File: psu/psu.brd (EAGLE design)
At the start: 31 x 67 mm, 8 parts

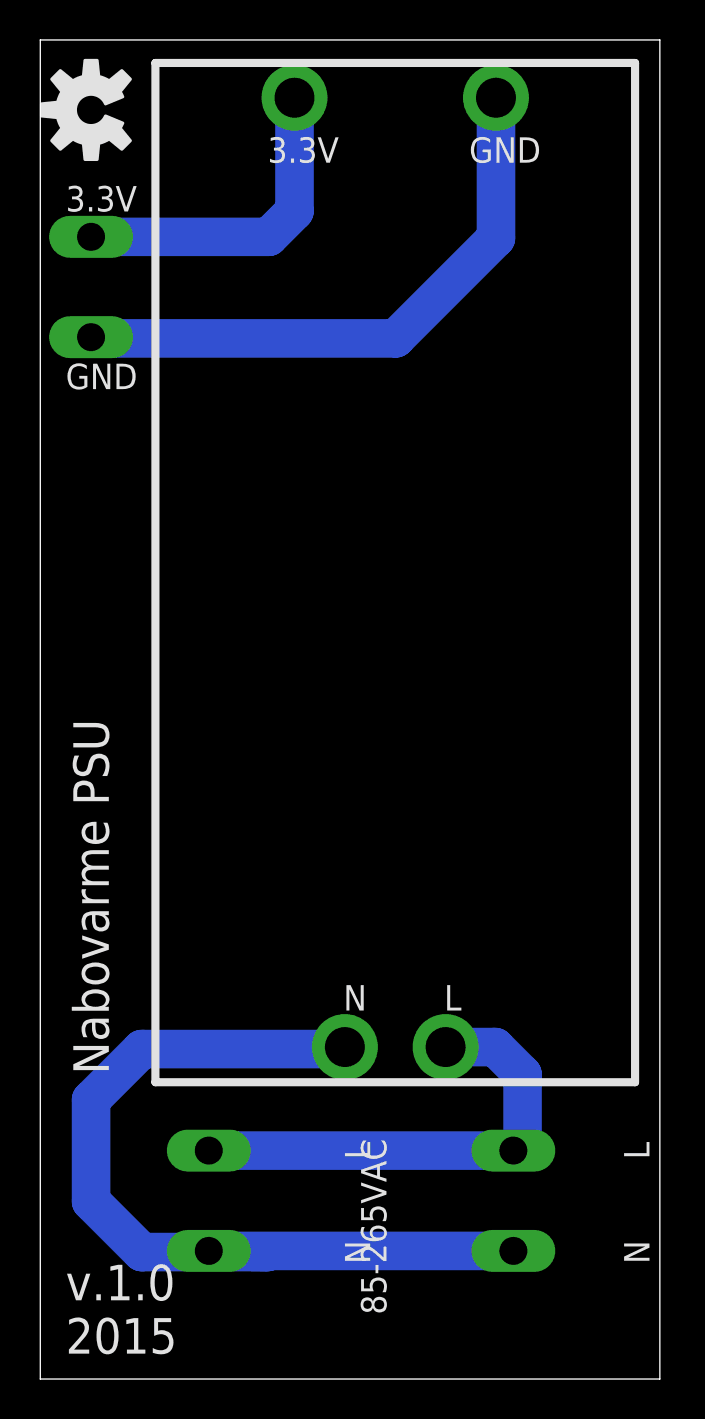
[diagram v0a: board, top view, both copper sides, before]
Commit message: psu pcb: v1.1
better placement of holes for psu module
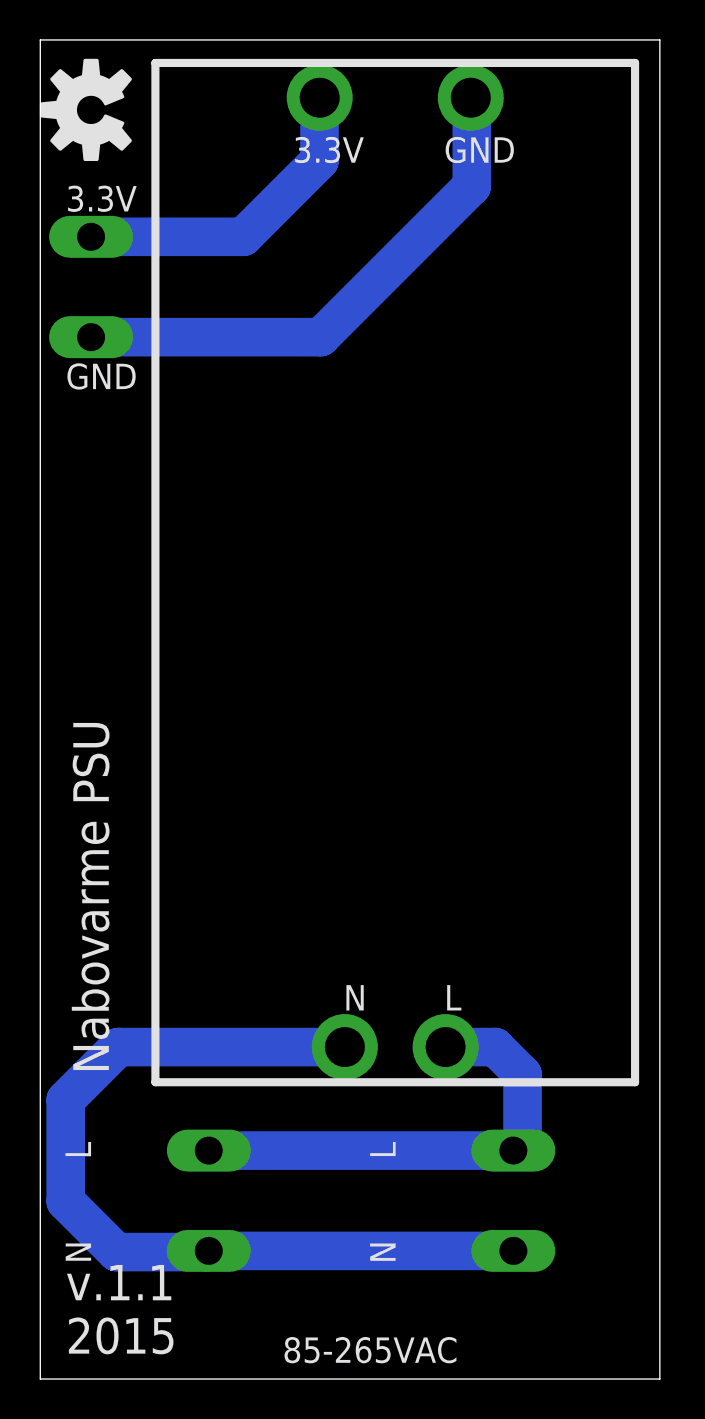
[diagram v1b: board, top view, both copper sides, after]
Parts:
- moved GND 1.26 mm to (21.5, 64.1)
- moved 3.3V 1.26 mm to (14.0, 64.1)
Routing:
- net N$2: track 46.9 -> 43.6 mm
- net N$4: track 29.4 -> 26.6 mm
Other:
- board text added: "v.1.1 2015"
- board text removed: "v.1.0 2015"
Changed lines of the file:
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@@
 <text x="1.27" y="58.42" size="1.27" layer="25">3.3V</text>
 <text x="1.27" y="50.8" size="1.27" layer="25" align="top-left">GND</text>
-<text x="1.27" y="1.27" size="1.778" layer="25">v.1.0
+<text x="1.27" y="1.27" size="1.778" layer="25">v.1.1
 2015</text>
-<text x="16.51" y="11.43" size="1.27" layer="25" rot="R270" align="top-center">L</text>
-<text x="16.51" y="6.35" size="1.27" layer="25" rot="R270" align="top-center">N</text>
-<text x="29.21" y="6.35" size="1.27" layer="25" rot="R90" align="top-center">N</text>
-<text x="29.21" y="11.43" size="1.27" layer="25" rot="R90" align="top-center">L</text>
+<text x="2.54" y="11.43" size="1.27" layer="25" rot="R270" align="top-center">L</text>
+<text x="2.54" y="6.35" size="1.27" layer="25" rot="R270" align="top-center">N</text>
+<text x="16.51" y="6.35" size="1.27" layer="25" rot="R90" align="top-center">N</text>
+<text x="16.51" y="11.43" size="1.27" layer="25" rot="R90" align="top-center">L</text>
 </plain>
 <attributes>
@@
 <attribute name="NAME" x="20.2038" y="18.4388" size="1.27" layer="25"/>
 </element>
-<element name="3.3V" library="SparkFun (old)" package="1X01_2MM" value="M01PTH_2MM" x="12.72" y="64.11" smashed="yes">
-<attribute name="NAME" x="11.3738" y="60.8588" size="1.27" layer="25"/>
-</element>
-<element name="GND" library="SparkFun (old)" package="1X01_2MM" value="M01PTH_2MM" x="22.8" y="64.11" smashed="yes">
-<attribute name="NAME" x="21.4538" y="60.8588" size="1.27" layer="25"/>
+<element name="3.3V" library="SparkFun (old)" package="1X01_2MM" value="M01PTH_2MM" x="13.98" y="64.11" smashed="yes">
+<attribute name="NAME" x="12.6338" y="60.8588" size="1.27" layer="25"/>
+</element>
+<element name="GND" library="SparkFun (old)" package="1X01_2MM" value="M01PTH_2MM" x="21.54" y="64.11" smashed="yes">
+<attribute name="NAME" x="20.1938" y="60.8588" size="1.27" layer="25"/>
 </element>
 <element name="85-265VAC" library="SparkFun (old)" package="1X02_LONGPADS" value="" x="23.67" y="11.43" smashed="yes" rot="R270">
-<attribute name="NAME" x="16.05" y="7.62" size="1.27" layer="25" rot="R270" align="bottom-center"/>
+<attribute name="NAME" x="16.51" y="0.81" size="1.27" layer="25" align="bottom-center"/>
 </element>
 <element name="JP2" library="SparkFun (old)" package="1X02_LONGPADS" value="" x="2.54" y="57.15" smashed="yes" rot="R270"/>
@@
 <contactref element="N" pad="1"/>
 <contactref element="85-265VAC1" pad="2"/>
-<wire x1="5.08" y1="6.35" x2="11.37" y2="6.35" width="1.9304" layer="16"/>
-<wire x1="11.37" y1="6.35" x2="8.43" y2="6.41" width="1.9304" layer="16"/>
-<wire x1="8.43" y1="6.41" x2="23.67" y2="6.41" width="1.9304" layer="16"/>
-<wire x1="5.08" y1="6.35" x2="2.54" y2="8.89" width="1.9304" layer="16"/>
-<wire x1="2.54" y1="8.89" x2="2.54" y2="13.97" width="1.9304" layer="16"/>
-<wire x1="2.54" y1="13.97" x2="5.08" y2="16.51" width="1.9304" layer="16"/>
-<wire x1="5.08" y1="16.51" x2="15.14" y2="16.51" width="1.9304" layer="16"/>
-<wire x1="15.14" y1="16.51" x2="15.24" y2="16.61" width="1.9304" layer="16"/>
+<wire x1="15.24" y1="16.61" x2="3.91" y2="16.61" width="1.9304" layer="16"/>
+<wire x1="3.91" y1="16.61" x2="1.27" y2="13.97" width="1.9304" layer="16"/>
+<wire x1="1.27" y1="13.97" x2="1.27" y2="8.89" width="1.9304" layer="16"/>
+<wire x1="1.27" y1="8.89" x2="3.81" y2="6.35" width="1.9304" layer="16"/>
+<wire x1="3.81" y1="6.35" x2="8.37" y2="6.35" width="1.9304" layer="16"/>
+<wire x1="8.37" y1="6.35" x2="8.43" y2="6.41" width="1.9304" layer="16"/>
+<wire x1="23.67" y1="6.41" x2="8.43" y2="6.41" width="1.9304" layer="16"/>
 </signal>
 <signal name="N$3">
 <contactref element="JP2" pad="1"/>
 <contactref element="3.3V" pad="1"/>
-<wire x1="12.72" y1="64.11" x2="12.72" y2="58.44" width="1.9304" layer="16"/>
-<wire x1="12.72" y1="58.44" x2="11.43" y2="57.15" width="1.9304" layer="16"/>
-<wire x1="11.43" y1="57.15" x2="2.54" y2="57.15" width="1.9304" layer="16"/>
+<wire x1="2.54" y1="57.15" x2="10.16" y2="57.15" width="1.9304" layer="16"/>
+<wire x1="10.16" y1="57.15" x2="13.97" y2="60.96" width="1.9304" layer="16"/>
+<wire x1="13.97" y1="60.96" x2="13.97" y2="64.1" width="1.9304" layer="16"/>
+<wire x1="13.97" y1="64.1" x2="13.98" y2="64.11" width="1.9304" layer="16"/>
 </signal>
 <signal name="N$4">
 <contactref element="JP2" pad="2"/>
 <contactref element="GND" pad="1"/>
-<wire x1="22.8" y1="64.11" x2="22.8" y2="57.09" width="1.9304" layer="16"/>
-<wire x1="22.8" y1="57.09" x2="17.78" y2="52.07" width="1.9304" layer="16"/>
-<wire x1="17.78" y1="52.07" x2="2.6" y2="52.07" width="1.9304" layer="16"/>
-<wire x1="2.6" y1="52.07" x2="2.54" y2="52.13" width="1.9304" layer="16"/>
+<wire x1="2.54" y1="52.13" x2="14.03" y2="52.13" width="1.9304" layer="16"/>
+<wire x1="14.03" y1="52.13" x2="21.59" y2="59.69" width="1.9304" layer="16"/>
+<wire x1="21.59" y1="59.69" x2="21.59" y2="64.06" width="1.9304" layer="16"/>
+<wire x1="21.59" y1="64.06" x2="21.54" y2="64.11" width="1.9304" layer="16"/>
 </signal>
 </signals>
